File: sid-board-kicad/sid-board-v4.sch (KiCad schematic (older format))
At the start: 52 parts, among them J1 SPI + UART, J2 USB_B_Micro, J3 Conn_01x08, Q1 BSS138, Q2 BSS138, SW1 SW_EN, SW2 SW_FLASH, U1 SC16IS762IBS, U2 MCP1703A-3302_SOT223, U3 SN65HVD232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

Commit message: Layer 4 stuff
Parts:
- removed D1: LED7, LED_SMD:LED_0805_2012Metric_Pad1.15x1.40mm_HandSolder, symbol Device:LED
- removed D2: LED6, LED_SMD:LED_0805_2012Metric_Pad1.15x1.40mm_HandSolder, symbol Device:LED
- removed D3: LED5, LED_SMD:LED_0805_2012Metric_Pad1.15x1.40mm_HandSolder, symbol Device:LED
- removed D4: LED4, LED_SMD:LED_0805_2012Metric_Pad1.15x1.40mm_HandSolder, symbol Device:LED
- removed D5: LED3, LED_SMD:LED_0805_2012Metric_Pad1.15x1.40mm_HandSolder, symbol Device:LED
- removed D6: LED2, LED_SMD:LED_0805_2012Metric_Pad1.15x1.40mm_HandSolder, symbol Device:LED
- removed D7: LED1, LED_SMD:LED_0805_2012Metric_Pad1.15x1.40mm_HandSolder, symbol Device:LED
- removed D8: LED0, LED_SMD:LED_0805_2012Metric_Pad1.15x1.40mm_HandSolder, symbol Device:LED
- removed J3: Conn_01x08, Connector_PinHeader_2.54mm:PinHeader_1x08_P2.54mm_Vertical, symbol Connector_Generic:Conn_01x08
- removed R18: 1K, Resistor_SMD:R_0805_2012Metric_Pad1.15x1.40mm_HandSolder, symbol Device:R_Small
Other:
- note removed: "GPIO LED OUTPUT"
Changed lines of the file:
@@
 Text GLabel 7750 2700 3    50   Input ~ 0
 XTAL1
-$Comp
-L Device:LED D1
-U 1 1 5E524EBA
-P 7100 1100
-F 0 "D1" H 7093 845 50  0000 C CNN
-F 1 "LED7" H 7093 936 50  0000 C CNN
-F 2 "LED_SMD:LED_0805_2012Metric_Pad1.15x1.40mm_HandSolder" H 7100 1100 50  0001 C CNN
-F 3 "~" H 7100 1100 50  0001 C CNN
-	1    7100 1100
-	-1   0    0    1
-$EndComp
-$Comp
-L Device:LED D2
-U 1 1 5E52A67D
-P 7100 1200
-F 0 "D2" H 7093 945 50  0000 C CNN
-F 1 "LED6" H 7093 1036 50  0000 C CNN
-F 2 "LED_SMD:LED_0805_2012Metric_Pad1.15x1.40mm_HandSolder" H 7100 1200 50  0001 C CNN
-F 3 "~" H 7100 1200 50  0001 C CNN
-	1    7100 1200
-	-1   0    0    1
-$EndComp
-$Comp
-L Device:LED D3
-U 1 1 5E52A91D
-P 7100 1300
-F 0 "D3" H 7093 1045 50  0000 C CNN
-F 1 "LED5" H 7093 1136 50  0000 C CNN
-F 2 "LED_SMD:LED_0805_2012Metric_Pad1.15x1.40mm_HandSolder" H 7100 1300 50  0001 C CNN
-F 3 "~" H 7100 1300 50  0001 C CNN
-	1    7100 1300
-	-1   0    0    1
-$EndComp
-$Comp
-L Device:LED D4
-U 1 1 5E52ACF3
-P 7100 1400
-F 0 "D4" H 7093 1145 50  0000 C CNN
-F 1 "LED4" H 7093 1236 50  0000 C CNN
-F 2 "LED_SMD:LED_0805_2012Metric_Pad1.15x1.40mm_HandSolder" H 7100 1400 50  0001 C CNN
-F 3 "~" H 7100 1400 50  0001 C CNN
-	1    7100 1400
-	-1   0    0    1
-$EndComp
-$Comp
-L Device:LED D5
-U 1 1 5E52AFBB
-P 7100 1800
-F 0 "D5" H 7093 1545 50  0000 C CNN
-F 1 "LED3" H 7093 1636 50  0000 C CNN
-F 2 "LED_SMD:LED_0805_2012Metric_Pad1.15x1.40mm_HandSolder" H 7100 1800 50  0001 C CNN
-F 3 "~" H 7100 1800 50  0001 C CNN
-	1    7100 1800
-	-1   0    0    1
-$EndComp
-$Comp
-L Device:LED D6
-U 1 1 5E52B30B
-P 7100 1900
-F 0 "D6" H 7093 1645 50  0000 C CNN
-F 1 "LED2" H 7093 1736 50  0000 C CNN
-F 2 "LED_SMD:LED_0805_2012Metric_Pad1.15x1.40mm_HandSolder" H 7100 1900 50  0001 C CNN
-F 3 "~" H 7100 1900 50  0001 C CNN
-	1    7100 1900
-	-1   0    0    1
-$EndComp
-$Comp
-L Device:LED D7
-U 1 1 5E52B635
-P 7100 2000
-F 0 "D7" H 7093 1745 50  0000 C CNN
-F 1 "LED1" H 7093 1836 50  0000 C CNN
-F 2 "LED_SMD:LED_0805_2012Metric_Pad1.15x1.40mm_HandSolder" H 7100 2000 50  0001 C CNN
-F 3 "~" H 7100 2000 50  0001 C CNN
-	1    7100 2000
-	-1   0    0    1
-$EndComp
-$Comp
-L Device:LED D8
-U 1 1 5E52B939
-P 7100 2100
-F 0 "D8" H 7093 1845 50  0000 C CNN
-F 1 "LED0" H 7093 1936 50  0000 C CNN
-F 2 "LED_SMD:LED_0805_2012Metric_Pad1.15x1.40mm_HandSolder" H 7100 2100 50  0001 C CNN
-F 3 "~" H 7100 2100 50  0001 C CNN
-	1    7100 2100
-	-1   0    0    1
-$EndComp
-$Comp
-L Device:R_Small R18
-U 1 1 5E53B9FC
-P 7350 1600
-F 0 "R18" H 7409 1646 50  0000 L CNN
-F 1 "1K" H 7409 1555 50  0000 L CNN
-F 2 "Resistor_SMD:R_0805_2012Metric_Pad1.15x1.40mm_HandSolder" H 7350 1600 50  0001 C CNN
-F 3 "~" H 7350 1600 50  0001 C CNN
-	1    7350 1600
-	0    -1   -1   0
-$EndComp
-Connection ~ 7250 1200
-Wire Wire Line
-	7250 1200 7250 1100
-Connection ~ 7250 1300
-Wire Wire Line
-	7250 1300 7250 1200
-Wire Wire Line
-	7250 1400 7250 1300
-Connection ~ 7250 1900
-Wire Wire Line
-	7250 1900 7250 1800
-Connection ~ 7250 2000
-Wire Wire Line
-	7250 2000 7250 1900
-Wire Wire Line
-	7250 2100 7250 2000
-Wire Notes Line
-	6700 850  7600 850
-Wire Notes Line
-	7600 2250 6700 2250
-Wire Notes Line
-	6700 2250 6700 850
-Text Notes 6700 800  0    50   ~ 0
-GPIO LED OUTPUT
 Text GLabel 4750 2400 0    50   Input ~ 0
 CLK
@@
 Wire Notes Line
 	4250 4500 2250 4500
-Wire Wire Line
-	7250 1600 7250 1400
-Connection ~ 7250 1400
-Wire Wire Line
-	7250 1600 7250 1800
-Connection ~ 7250 1600
-Connection ~ 7250 1800
-Wire Notes Line
-	7600 850  7600 2250
 $Comp
 L Device:C_Small C6
@@
 	1    0    0    -1
 $EndComp
-$Comp
-L Connector_Generic:Conn_01x08 J3
-U 1 1 5F374BE1
-P 5400 7350
-F 0 "J3" V 5525 7296 50  0000 C CNN
-F 1 "Conn_01x08" V 5616 7296 50  0000 C CNN
-F 2 "Connector_PinHeader_2.54mm:PinHeader_1x08_P2.54mm_Vertical" H 5400 7350 50  0001 C CNN
-F 3 "~" H 5400 7350 50  0001 C CNN
-	1    5400 7350
-	0    1    1    0
-$EndComp
 Text GLabel 5900 5350 2    50   Input ~ 0
 I2S_DIN
@@
 Text GLabel 5900 5650 2    50   Input ~ 0
 I2S_BCLK
-Text GLabel 5200 7150 1    50   Input ~ 0
-I2S_DIN
-Text GLabel 5100 7150 1    50   Input ~ 0
-I2S_WSEL
-Text GLabel 5000 7150 1    50   Input ~ 0
-I2S_BCLK
-Wire Wire Line
-	5900 5950 5400 5950
-Wire Wire Line
-	5400 5950 5400 7150
-Wire Wire Line
-	5900 5850 5500 5850
-Wire Wire Line
-	5500 5850 5500 7150
-Wire Wire Line
-	5900 5750 5350 5750
-Wire Wire Line
-	5350 5750 5350 7150
-Wire Wire Line
-	5350 7150 5300 7150
-Wire Notes Line
-	4850 6650 5850 6650
-Wire Notes Line
-	5850 6650 5850 7650
-Wire Notes Line
-	5850 7650 4850 7650
-Wire Notes Line
-	4850 7650 4850 6650
 Text GLabel 10000 4650 3    50   Input ~ 0
 RX_ESP32
@@
 $EndComp
 $Comp
-L power:GND #PWR0120
-U 1 1 5F547763
-P 7450 1600
-F 0 "#PWR0120" H 7450 1350 50  0001 C CNN
-F 1 "GND" H 7455 1427 50  0000 C CNN
-F 2 "" H 7450 1600 50  0001 C CNN
-F 3 "" H 7450 1600 50  0001 C CNN
-	1    7450 1600
-	1    0    0    -1
-$EndComp
-$Comp
 L power:GND #PWR0121
 U 1 1 5F549615
@@
 Connection ~ 5300 3650
 $Comp
-L power:+3.3V #PWR0134
-U 1 1 5F572C6A
-P 5600 7150
-F 0 "#PWR0134" H 5600 7000 50  0001 C CNN
-F 1 "+3.3V" H 5615 7323 50  0000 C CNN
-F 2 "" H 5600 7150 50  0001 C CNN
-F 3 "" H 5600 7150 50  0001 C CNN
-	1    5600 7150
-	1    0    0    -1
-$EndComp
-$Comp
-L power:GND #PWR0135
-U 1 1 5F573E82
-P 5700 7150
-F 0 "#PWR0135" H 5700 6900 50  0001 C CNN
-F 1 "GND" H 5705 6977 50  0000 C CNN
-F 2 "" H 5700 7150 50  0001 C CNN
-F 3 "" H 5700 7150 50  0001 C CNN
-	1    5700 7150
-	-1   0    0    1
-$EndComp
-$Comp
 L power:+3.3V #PWR0136

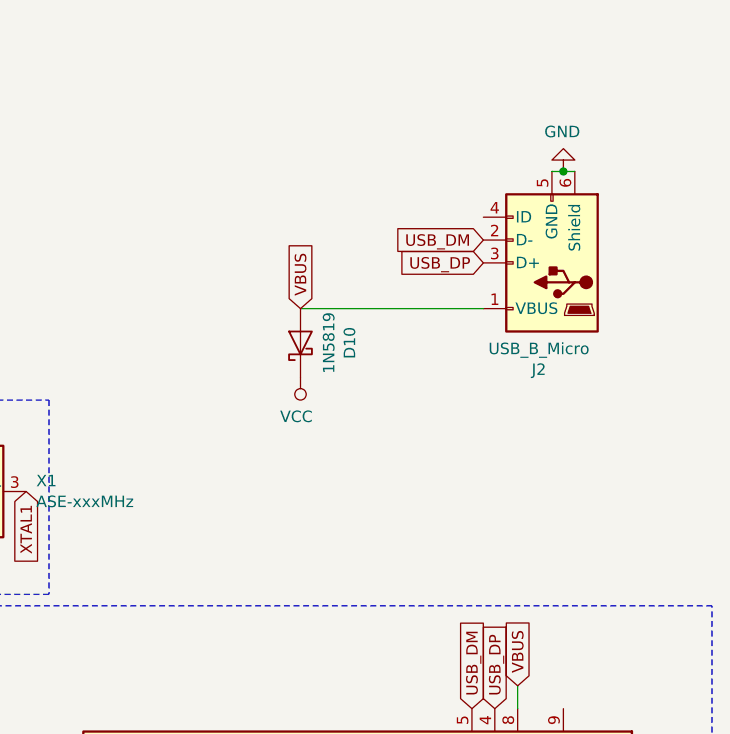
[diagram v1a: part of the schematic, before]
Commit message: Added USBC port which I know exists
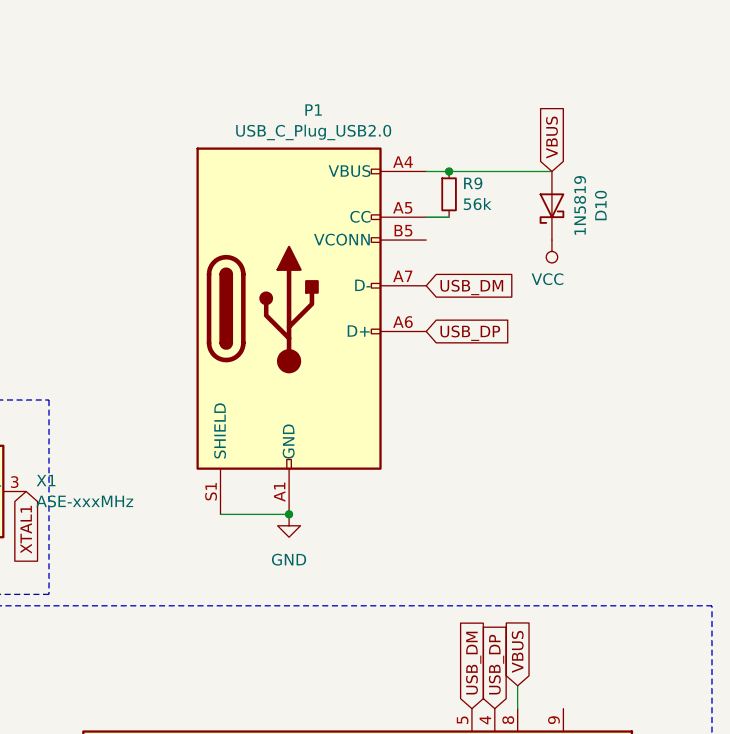
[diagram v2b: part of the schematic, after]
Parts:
- removed J2: USB_B_Micro, Connector_USB:USB_Micro-B_Molex-105017-0001, symbol Connector:USB_B_Micro
- added P1: USB_C_Plug_USB2.0, Connector_USB:USB_C_Receptacle_Amphenol_12401610E4-2A, symbol Connector:USB_C_Plug_USB2.0
- added R9: 56k, Resistor_SMD:R_0805_2012Metric_Pad1.15x1.40mm_HandSolder, symbol Device:R_Small
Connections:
- net GND: now also P1.A1 (GND), P1.A12 (GND), P1.B1 (GND), P1.B12 (GND), P1.S1 (SHIELD)
- net USB_DM: now also P1.A7 (D-)
- net USB_DP: now also P1.A6 (D+)
- net VBUS: now also P1.A4 (VBUS), P1.A9 (VBUS), P1.B4 (VBUS), P1.B9 (VBUS), R9.1
- new net: P1.A5 (CC), R9.2
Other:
- moved on the sheet: D10
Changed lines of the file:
@@
 IO0
-$Comp
-L Connector:USB_B_Micro J2
-U 1 1 5F431498
-P 10050 1700
-F 0 "J2" H 10107 2167 50  0000 C CNN
-F 1 "USB_B_Micro" H 10107 2076 50  0000 C CNN
-F 2 "Connector_USB:USB_Micro-B_Molex-105017-0001" H 10200 1650 50  0001 C CNN
-F 3 "~" H 10200 1650 50  0001 C CNN
-	1    10050 1700
-	-1   0    0    1
-$EndComp
-$Comp
-L Diode:1N5819 D10
-U 1 1 5F43801F
-P 8950 2050
-F 0 "D10" H 8950 1834 50  0000 C CNN
-F 1 "1N5819" H 8950 1925 50  0000 C CNN
-F 2 "Diode_SMD:D_SOD-123" H 8950 1875 50  0001 C CNN
-F 3 "http://www.vishay.com/docs/88525/1n5817.pdf" H 8950 2050 50  0001 C CNN
-	1    8950 2050
-	0    -1   -1   0
-$EndComp
-Wire Wire Line
-	10150 1300 10100 1300
 $Comp
 L Device:LED_Small D9
@@
 Text GLabel 5900 3950 2    50   Input ~ 0
 TX_ESP32
-Text GLabel 9750 1700 0    50   Input ~ 0
+Text GLabel 9500 2000 2    50   Input ~ 0
 USB_DP
-Text GLabel 9750 1600 0    50   Input ~ 0
+Text GLabel 9500 1800 2    50   Input ~ 0
 USB_DM
 Text GLabel 9700 3650 1    50   Input ~ 0
@@
 Text GLabel 9800 3650 1    50   Input ~ 0
 USB_DP
-Text GLabel 8950 1900 1    50   Input ~ 0
-VBUS
 Text GLabel 9900 3550 1    50   Input ~ 0
 VBUS
@@
 Wire Notes Line
 	4300 3200 10750 3200
-Wire Wire Line
-	8950 1900 9750 1900
 Text GLabel 1150 3700 0    50   Input ~ 0
 CAN_H
@@
 L power:GND #PWR0128
 U 1 1 5F555477
-P 10100 1300
-F 0 "#PWR0128" H 10100 1050 50  0001 C CNN
-F 1 "GND" H 10105 1127 50  0000 C CNN
-F 2 "" H 10100 1300 50  0001 C CNN
-F 3 "" H 10100 1300 50  0001 C CNN
-	1    10100 1300
-	-1   0    0    1
-$EndComp
-Connection ~ 10100 1300
-Wire Wire Line
-	10100 1300 10050 1300
-$Comp
-L power:VCC #PWR0129
-U 1 1 5F55A24A
-P 8950 2200
-F 0 "#PWR0129" H 8950 2050 50  0001 C CNN
-F 1 "VCC" H 8968 2373 50  0000 C CNN
-F 2 "" H 8950 2200 50  0001 C CNN
-F 3 "" H 8950 2200 50  0001 C CNN
-	1    8950 2200
-	-1   0    0    1
+P 8900 2800
+F 0 "#PWR0128" H 8900 2550 50  0001 C CNN
+F 1 "GND" H 8900 2600 50  0000 C CNN
+F 2 "" H 8900 2800 50  0001 C CNN
+F 3 "" H 8900 2800 50  0001 C CNN
+	1    8900 2800
+	1    0    0    -1
 $EndComp
 $Comp
@@
 	1    0    0    -1
 $EndComp
+$Comp
+L Connector:USB_C_Plug_USB2.0 P1
+U 1 1 5F5BFB7F
+P 8900 1900
+F 0 "P1" H 9007 2767 50  0000 C CNN
+F 1 "USB_C_Plug_USB2.0" H 9007 2676 50  0000 C CNN
+F 2 "Connector_USB:USB_C_Receptacle_Amphenol_12401610E4-2A" H 9050 1900 50  0001 C CNN
+F 3 "https://www.usb.org/sites/default/files/documents/usb_type-c.zip" H 9050 1900 50  0001 C CNN
+	1    8900 1900
+	1    0    0    -1
+$EndComp
+$Comp
+L power:VCC #PWR0129
+U 1 1 5F55A24A
+P 10050 1600
+F 0 "#PWR0129" H 10050 1450 50  0001 C CNN
+F 1 "VCC" H 10068 1773 50  0000 C CNN
+F 2 "" H 10050 1600 50  0001 C CNN
+F 3 "" H 10050 1600 50  0001 C CNN
+	1    10050 1600
+	-1   0    0    1
+$EndComp
+Text GLabel 10050 1300 1    50   Input ~ 0
+VBUS
+$Comp
+L Diode:1N5819 D10
+U 1 1 5F43801F
+P 10050 1450
+F 0 "D10" H 10050 1234 50  0000 C CNN
+F 1 "1N5819" H 10050 1325 50  0000 C CNN
+F 2 "Diode_SMD:D_SOD-123" H 10050 1275 50  0001 C CNN
+F 3 "http://www.vishay.com/docs/88525/1n5817.pdf" H 10050 1450 50  0001 C CNN
+	1    10050 1450
+	0    -1   -1   0
+$EndComp
+Wire Wire Line
+	10050 1300 9600 1300
+Wire Wire Line
+	8900 2800 8600 2800
+Connection ~ 8900 2800
+$Comp
+L Device:R_Small R9
+U 1 1 5F5C3392
+P 9600 1400
+F 0 "R9" H 9659 1446 50  0000 L CNN
+F 1 "56k" H 9659 1355 50  0000 L CNN
+F 2 "Resistor_SMD:R_0805_2012Metric_Pad1.15x1.40mm_HandSolder" H 9600 1400 50  0001 C CNN
+F 3 "~" H 9600 1400 50  0001 C CNN
+	1    9600 1400
+	1    0    0    -1
+$EndComp
+Connection ~ 9600 1300
+Wire Wire Line
+	9600 1300 9500 1300
+Wire Wire Line
+	9600 1500 9500 1500
 $EndSCHEMATC
